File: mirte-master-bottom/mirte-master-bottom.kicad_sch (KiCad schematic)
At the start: 9 parts, among them J13 oled_conn, Q1 DMG2305UX

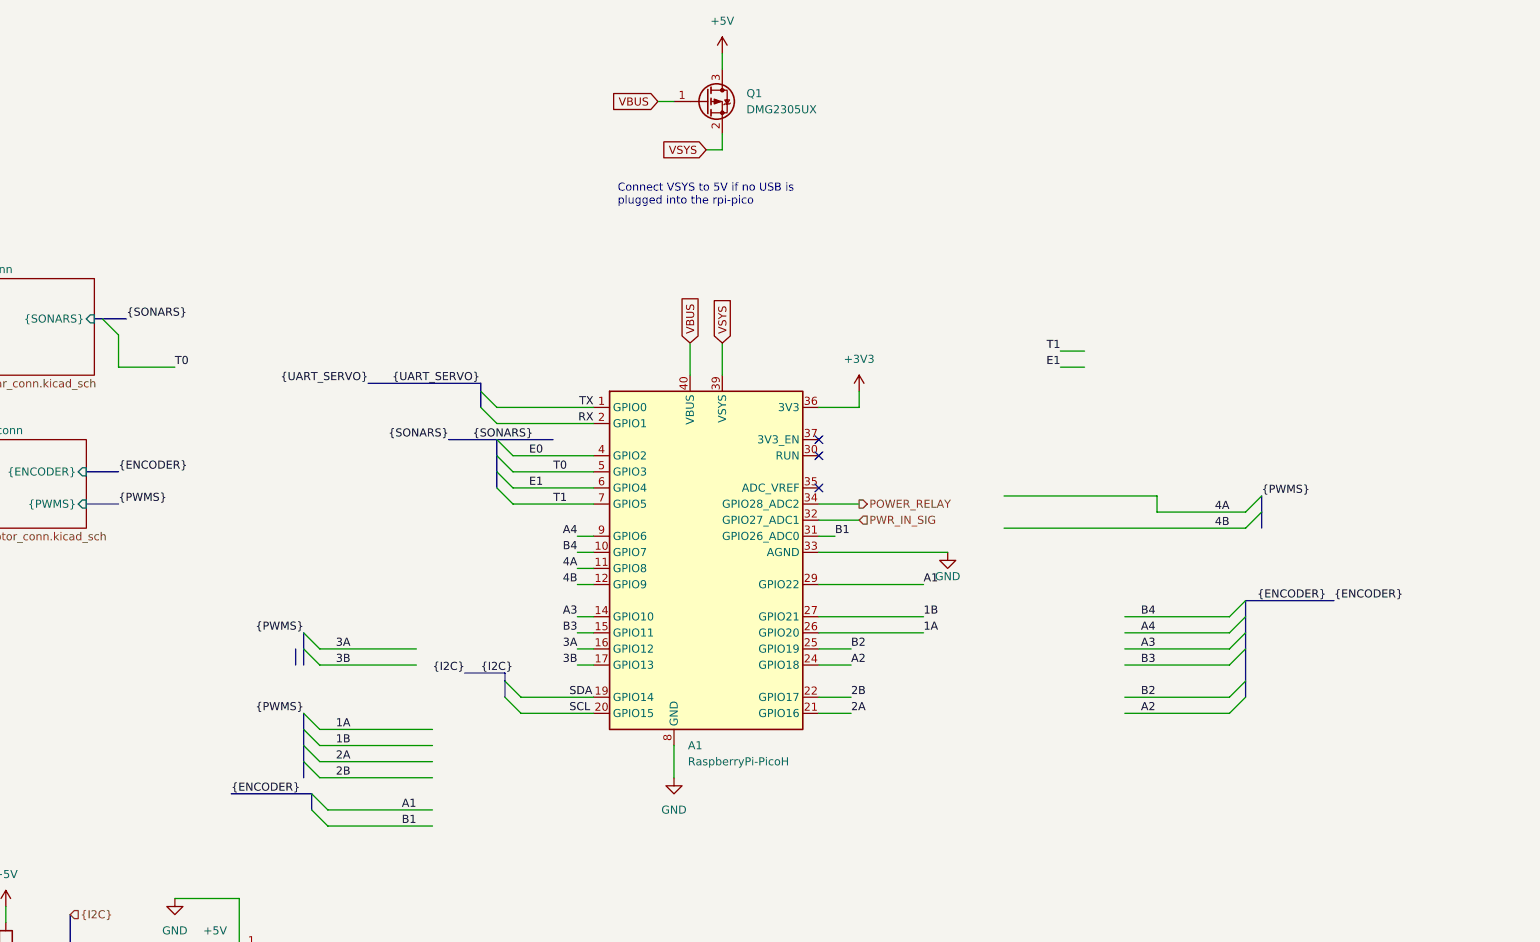
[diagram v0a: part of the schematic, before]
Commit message: reorder for i2c
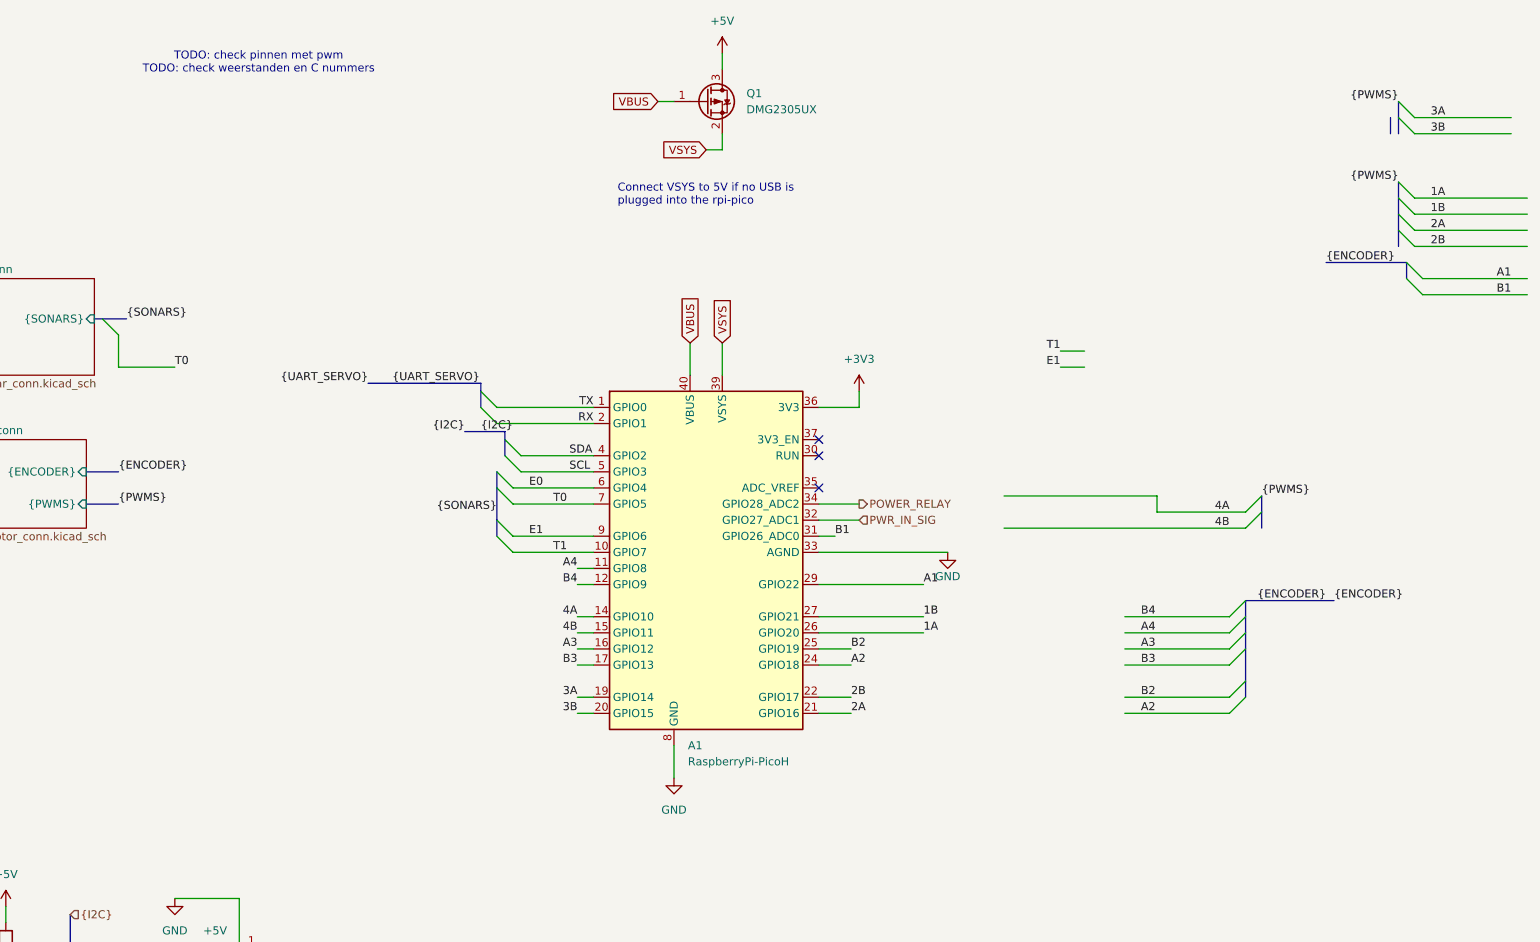
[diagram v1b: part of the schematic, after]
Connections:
- net 3A: now also A1.19 (GPIO14); no longer A1.16 (GPIO12)
- net 3B: now also A1.20 (GPIO15); no longer A1.17 (GPIO13)
- net 4A: now also A1.14 (GPIO10); no longer A1.11 (GPIO8)
- net 4B: now also A1.15 (GPIO11); no longer A1.12 (GPIO9)
- net A3: now also A1.16 (GPIO12); no longer A1.14 (GPIO10)
- net A4: now also A1.11 (GPIO8); no longer A1.9 (GPIO6)
- net B3: now also A1.17 (GPIO13); no longer A1.15 (GPIO11)
- net B4: now also A1.12 (GPIO9); no longer A1.10 (GPIO7)
- net E0: now also A1.6 (GPIO4); no longer A1.4 (GPIO2)
- net E1: now also A1.9 (GPIO6); no longer A1.6 (GPIO4)
- net SCL: now also A1.5 (GPIO3); no longer A1.20 (GPIO15)
- net SDA: now also A1.4 (GPIO2); no longer A1.19 (GPIO14)
- net T0: now also A1.7 (GPIO5); no longer A1.5 (GPIO3)
- net T1: now also A1.10 (GPIO7); no longer A1.7 (GPIO5)
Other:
- note added: "TODO: check pinnen met pwm TODO: check weerstanden en C nummers"

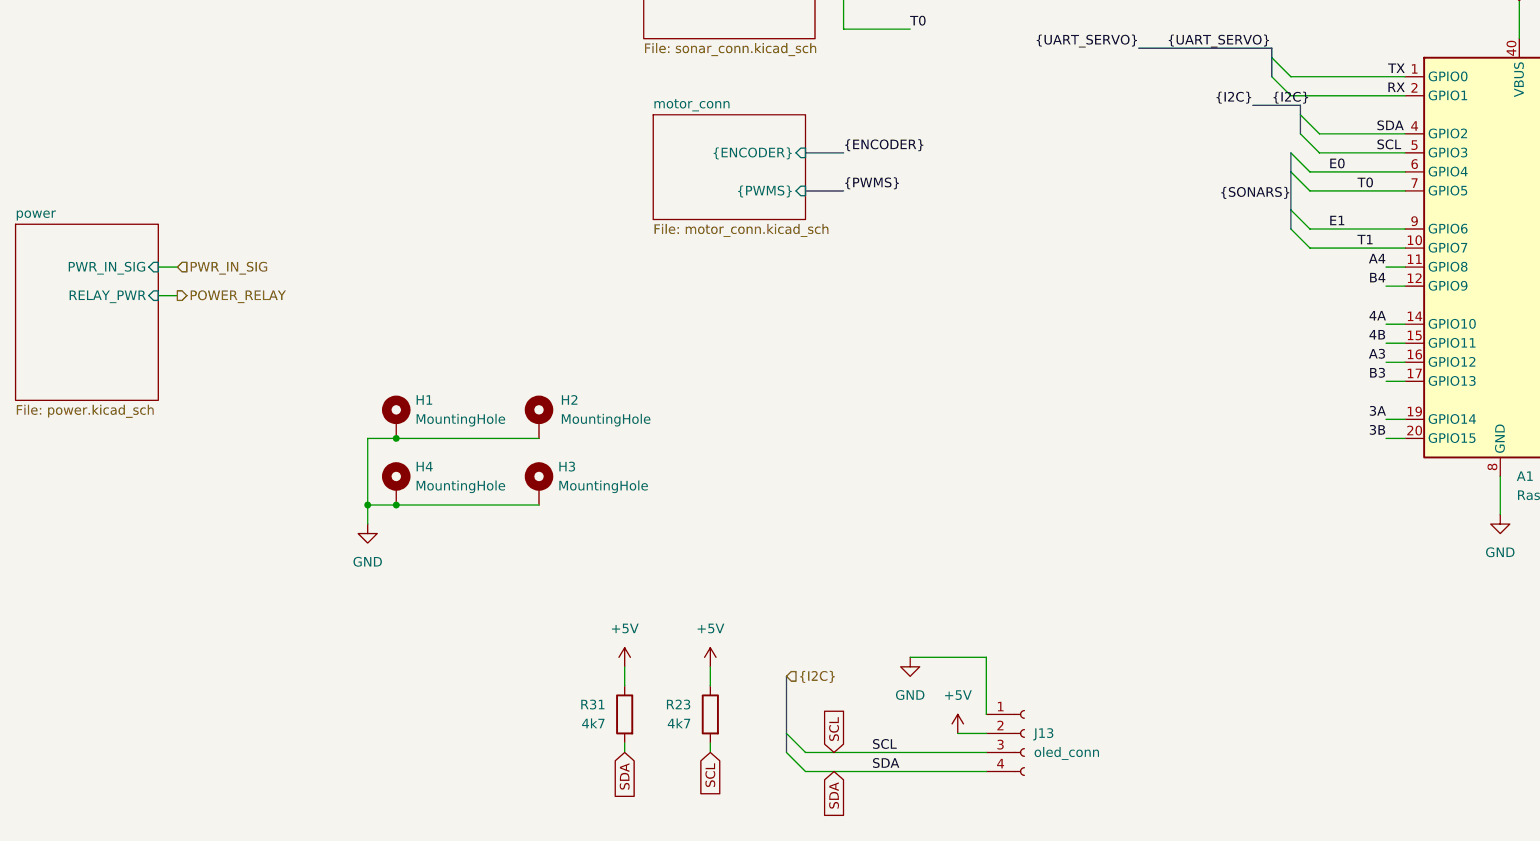
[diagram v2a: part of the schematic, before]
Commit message: master v3 sonar single pin
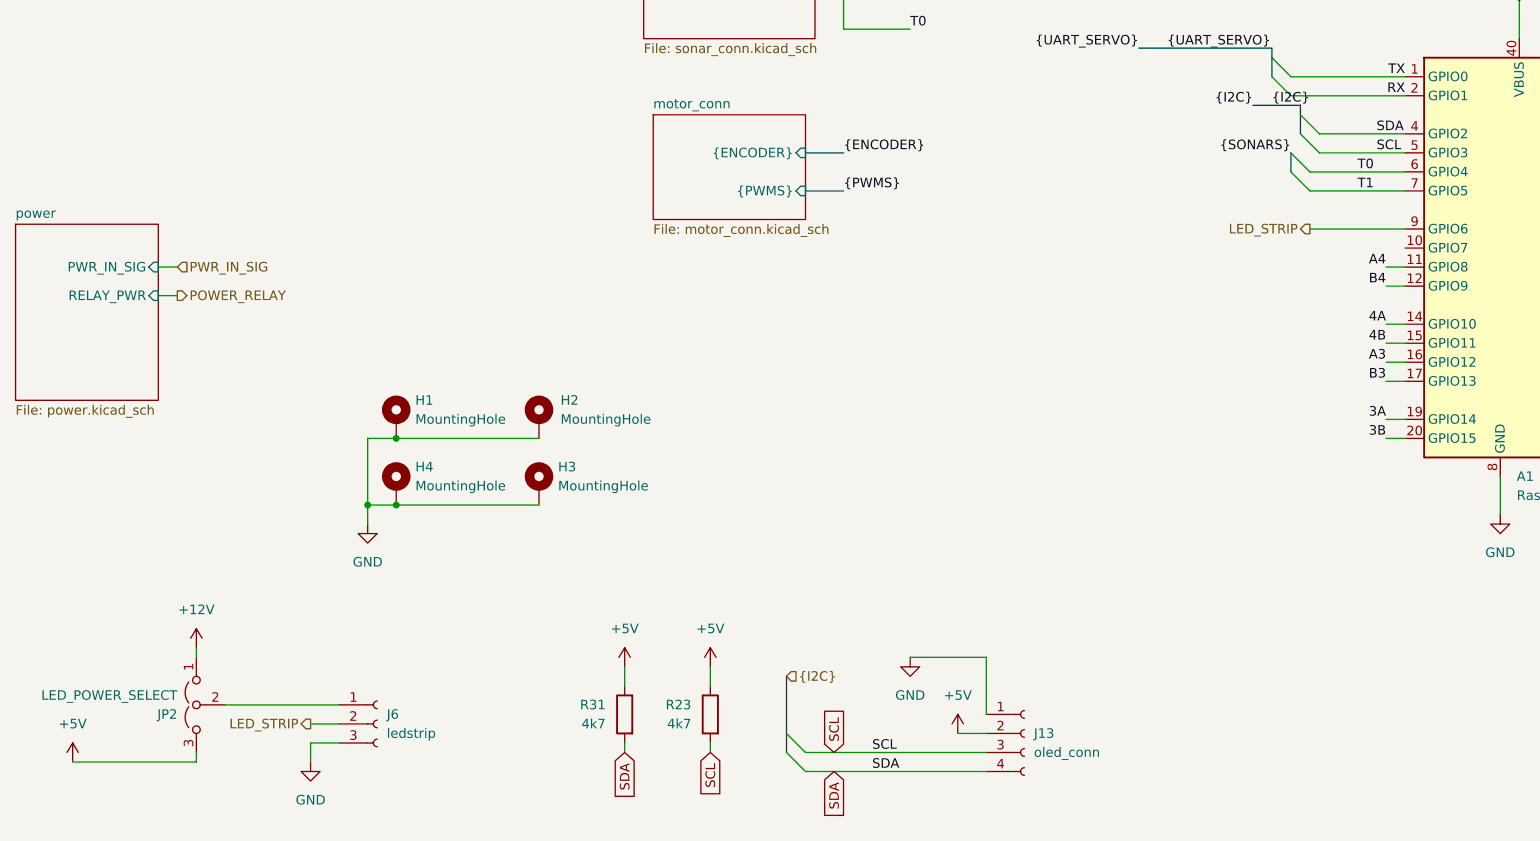
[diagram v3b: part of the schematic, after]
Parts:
- added J6: ledstrip, Connector_PinHeader_2.54mm:PinHeader_1x03_P2.54mm_Vertical, symbol Connector:Conn_01x03_Socket
- added JP2: LED_POWER_SELECT, Jumper:SolderJumper-3_P1.3mm_Bridged12_RoundedPad1.0x1.5mm_NumberLabels, symbol Jumper:Jumper_3_Open
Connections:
- net E0 is gone; now on net T0: A1.6 (GPIO4)
- net +5V: now also JP2.3 (B)
- net E1: no longer A1.9 (GPIO6)
- net GND: now also J6.3 (Pin_3)
- net T0: no longer A1.7 (GPIO5)
- net T1: now also A1.7 (GPIO5); no longer A1.10 (GPIO7)
- new net: J6.1 (Pin_1), JP2.2 (C)
- new net +12V: JP2.1 (A)
- new net LED_STRIP: A1.9 (GPIO6), J6.2 (Pin_2)

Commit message: mm v3 clean up board
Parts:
- added D10: LED, LED_SMD:LED_0805_2012Metric, symbol Device:LED
- added R34: ~600R, Resistor_SMD:R_0805_2012Metric, symbol Device:R
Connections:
- net GND: now also D10.1 (K)
- net GPIO7: now reaches A1.10 (GPIO7)
- net GPIO7: now also R34.1
- net RUN: now reaches A1.30 (RUN)
- net ADC_VREF: now reaches A1.35 (ADC_VREF)
- net 3v3EN: now reaches A1.37 (3V3_EN)
- new net: D10.2 (A), R34.2
- no-connect marks 3 -> 0

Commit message: mmv3 ordered pcb 2025-11-21
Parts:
- H1, H2, H3, H4: footprint MountingHole:MountingHole_3.2mm_M3_DIN965_Pad -> MountingHole:MountingHole_4.3mm_M4_DIN965_Pad
- R34: value ~600R -> 390
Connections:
- net GPIO7: now also R34.2; no longer R34.1
- net at D10.2 (A): now also R34.1; no longer R34.2
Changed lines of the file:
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@@
 			)
 		)
-		(property "Footprint" "MountingHole:MountingHole_3.2mm_M3_DIN965_Pad"
+		(property "Footprint" "MountingHole:MountingHole_4.3mm_M4_DIN965_Pad"
 			(at 71.12 134.62 0)
 			(effects
@@
 			)
 		)
-		(property "Footprint" "MountingHole:MountingHole_3.2mm_M3_DIN965_Pad"
+		(property "Footprint" "MountingHole:MountingHole_4.3mm_M4_DIN965_Pad"
 			(at 71.12 143.51 0)
 			(effects
@@
 			)
 		)
-		(property "Footprint" "MountingHole:MountingHole_3.2mm_M3_DIN965_Pad"
+		(property "Footprint" "MountingHole:MountingHole_4.3mm_M4_DIN965_Pad"
 			(at 90.17 134.62 0)
 			(effects
@@
 	(symbol
 		(lib_id "Device:R")
-		(at 162.56 130.81 0)
-		(unit 1)
-		(exclude_from_sim no)
-		(in_bom yes)
-		(on_board yes)
-		(dnp no)
-		(fields_autoplaced yes)
+		(at 162.56 130.81 180)
+		(unit 1)
+		(exclude_from_sim no)
+		(in_bom yes)
+		(on_board yes)
+		(dnp no)
 		(property "Reference" "R34"
 			(at 165.1 129.5399 0)
@@
 					(size 1.27 1.27)
 				)
-				(justify left)
-			)
-		)
-		(property "Value" "~600R"
+				(justify right)
+			)
+		)
+		(property "Value" "390"
 			(at 165.1 132.0799 0)
 			(effects
@@
 					(size 1.27 1.27)
 				)
-				(justify left)
+				(justify right)
 			)
 		)
 		(property "Footprint" "Resistor_SMD:R_0805_2012Metric"
-			(at 160.782 130.81 90)
+			(at 164.338 130.81 90)
 			(effects
 				(font
@@
 			)
 		)
-		(property "Description" ""
+		(property "Description" "Resistor"
 			(at 162.56 130.81 0)
 			(effects
@@
 			)
 		)
-		(property "Footprint" "MountingHole:MountingHole_3.2mm_M3_DIN965_Pad"
+		(property "Footprint" "MountingHole:MountingHole_4.3mm_M4_DIN965_Pad"
 			(at 90.17 143.51 0)
 			(effects

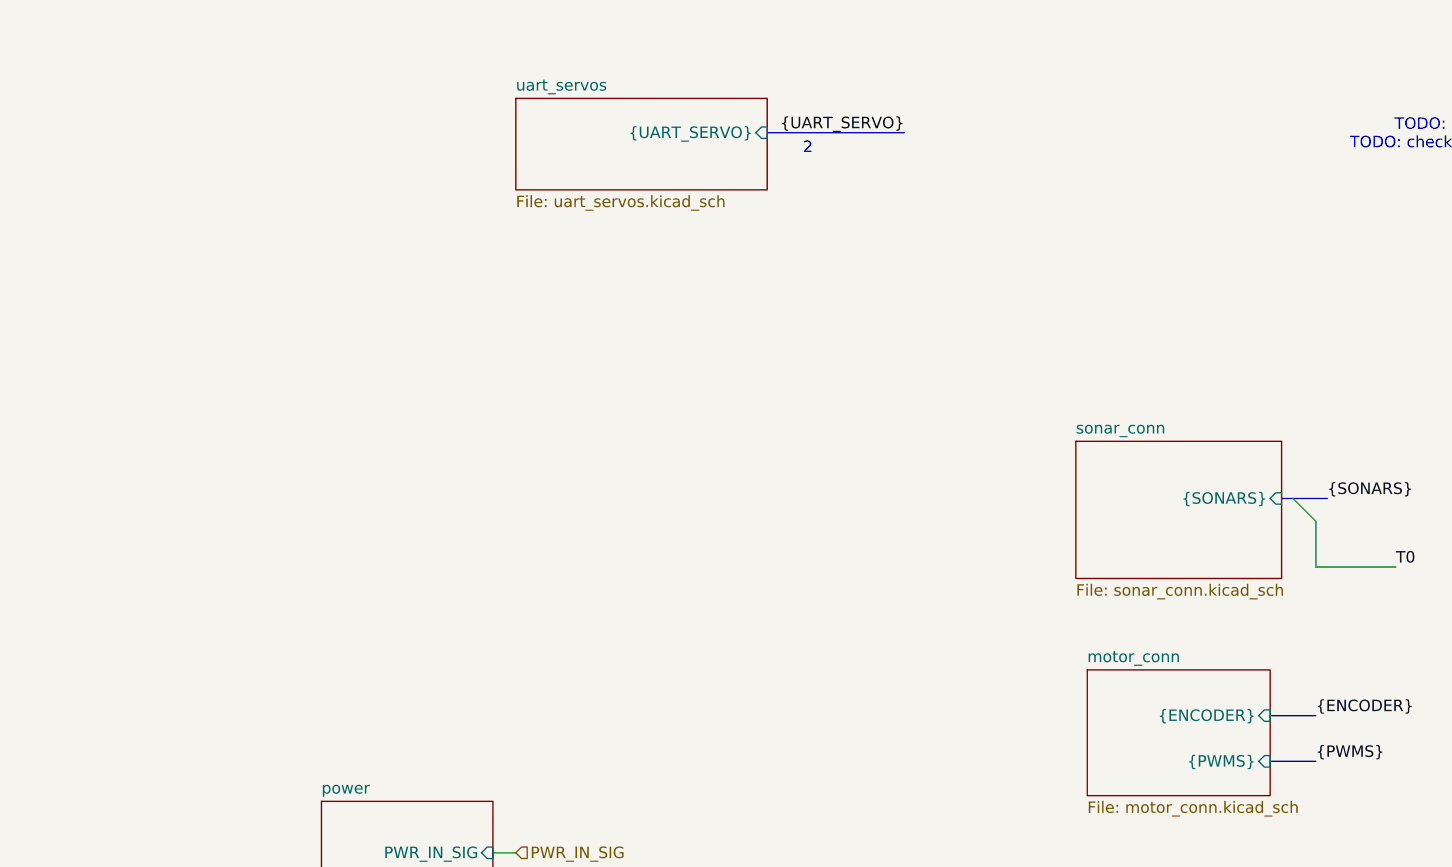
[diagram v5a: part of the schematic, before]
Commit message: Add emergency switch by using mosfet for power
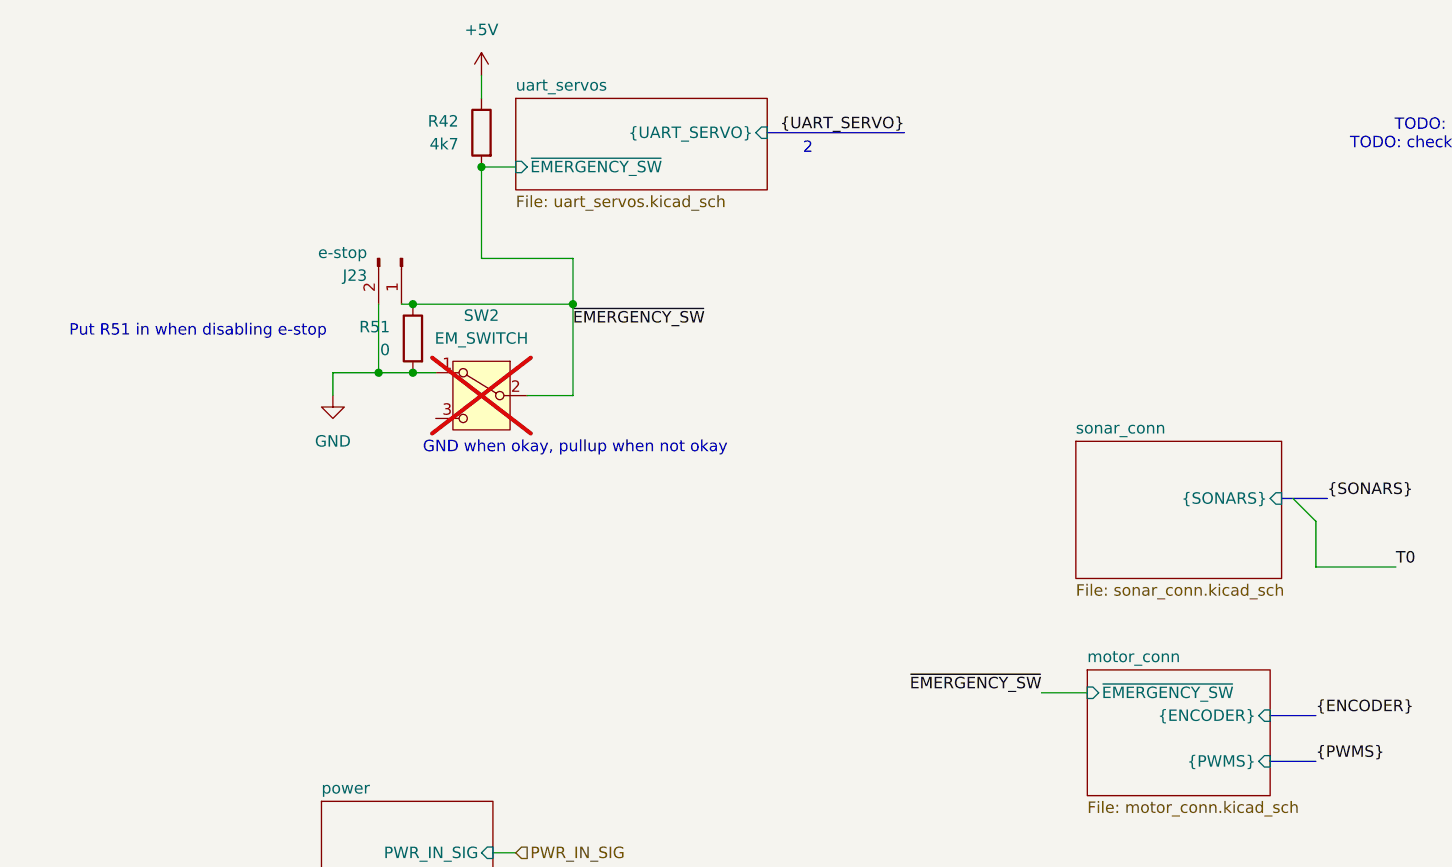
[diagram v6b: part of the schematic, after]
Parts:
- added J23: e-stop, Connector_JST:JST_XH_B2B-XH-AM_1x02_P2.50mm_Vertical, symbol Connector:Conn_01x02_Pin
- added R42: 4k7, Resistor_SMD:R_0805_2012Metric, symbol Device:R
- added R51: 0, Resistor_SMD:R_0805_2012Metric, symbol Device:R
- added SW2: EM_SWITCH, symbol Switch:SW_SPDT
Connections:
- net +5V: now also R42.1
- net GND: now also J23.2 (Pin_2), R51.2, SW2.1 (A)
- new net ~{EMERGENCY_SW}: J23.1 (Pin_1), R42.2, R51.1, SW2.2 (B)
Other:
- sheet motor_conn ports: added ~{EMERGENCY_SW}; removed none
- sheet uart_servos ports: added ~{EMERGENCY_SW}; removed none
- note added: "GND when okay, pullup when not okay"
- note added: "Put R51 in when disabling e-stop"
